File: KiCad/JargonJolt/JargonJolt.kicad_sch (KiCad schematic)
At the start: 7 parts

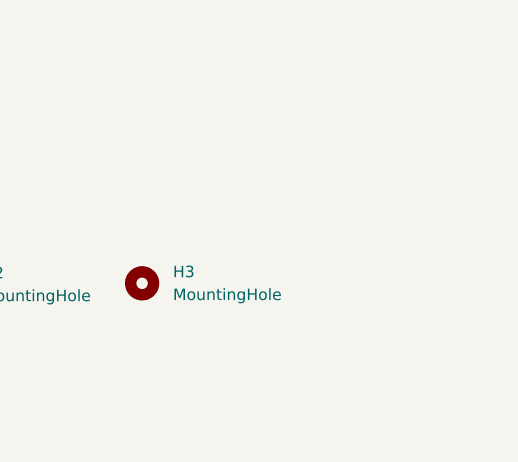
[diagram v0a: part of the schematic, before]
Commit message: added test leds
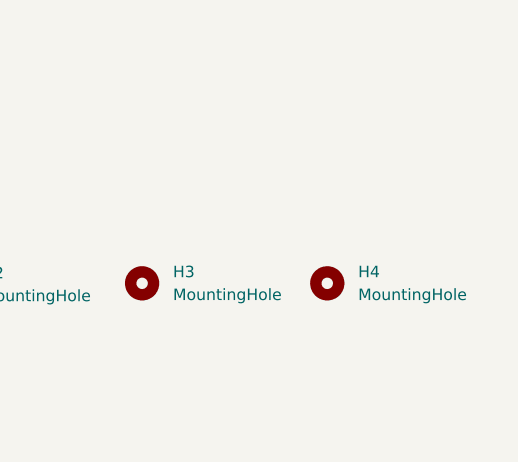
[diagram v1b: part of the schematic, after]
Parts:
- added H4: MountingHole, MountingHole:MountingHole_2.2mm_M2, symbol Mechanical:MountingHole
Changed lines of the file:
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@@
+    )
+  )
+  (symbol (lib_id "Mechanical:MountingHole") (at 252.73 124.46 0) (unit 1)
+    (in_bom yes) (on_board yes) (dnp no) (fields_autoplaced)
+    (property "Reference" "H4" (at 256.159 123.19 0)
+      (effects (font (size 1.27 1.27)) (justify left))
+    )
+    (property "Value" "MountingHole" (at 256.159 125.73 0)
+      (effects (font (size 1.27 1.27)) (justify left))
+    )
+    (property "Footprint" "MountingHole:MountingHole_2.2mm_M2" (at 252.73 124.46 0)
+      (effects (font (size 1.27 1.27)) hide)
+    )
+    (property "Datasheet" "~" (at 252.73 124.46 0)
+      (effects (font (size 1.27 1.27)) hide)
+    )
+    (instances
+      (project "JargonJolt"
+        (path "/39fa52d1-bab8-41e3-aba2-e2f783adaf1f"
+          (reference "H4") (unit 1)
+        )
+      )
     )
   )
